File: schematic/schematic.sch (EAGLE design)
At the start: 24 parts, among them J2 SJ-2523-SMT-TR

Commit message: Audio recording schematic update
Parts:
- added MICRO_SD_MODULE: (no value), pinhead:PINHD-1X6
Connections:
- removed net N$2: J2.TIP, U$1.L
- new net AUDIO: ARDUINO_NANO_AUDIO_CONTROLLER.A7, J2.TIP, U$1.L
- new net AUDIO_PASS: ARDUINO_NANO_AUDIO_CONTROLLER.D9
- new net MISO: ARDUINO_NANO_AUDIO_CONTROLLER.D12, MICRO_SD_MODULE.4
- new net MOSI: ARDUINO_NANO_AUDIO_CONTROLLER.D11, MICRO_SD_MODULE.3
- new net SCK: ARDUINO_NANO_AUDIO_CONTROLLER.D13, MICRO_SD_MODULE.2
- new net SS: ARDUINO_NANO_AUDIO_CONTROLLER.D10, MICRO_SD_MODULE.1
- net GND: now also MICRO_SD_MODULE.6
- net VCC: now also MICRO_SD_MODULE.5
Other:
- moved on the sheet: ARDUINO_NANO_AUDIO_CONTROLLER

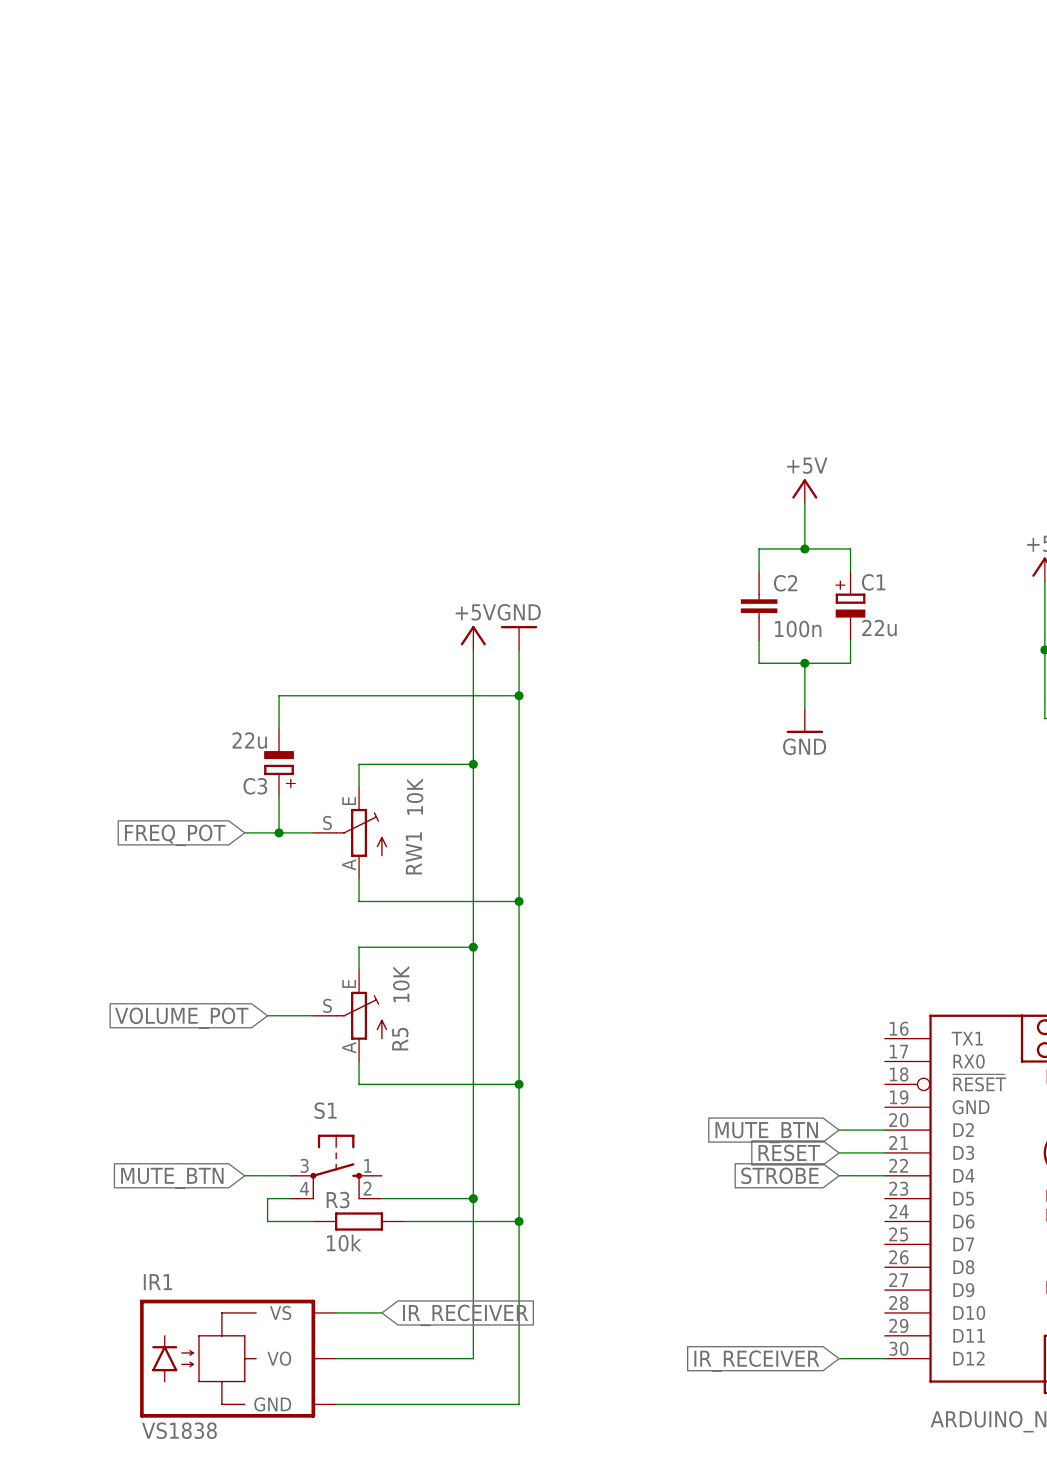
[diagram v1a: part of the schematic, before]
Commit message: Updated schematic with start/stop recording buttons
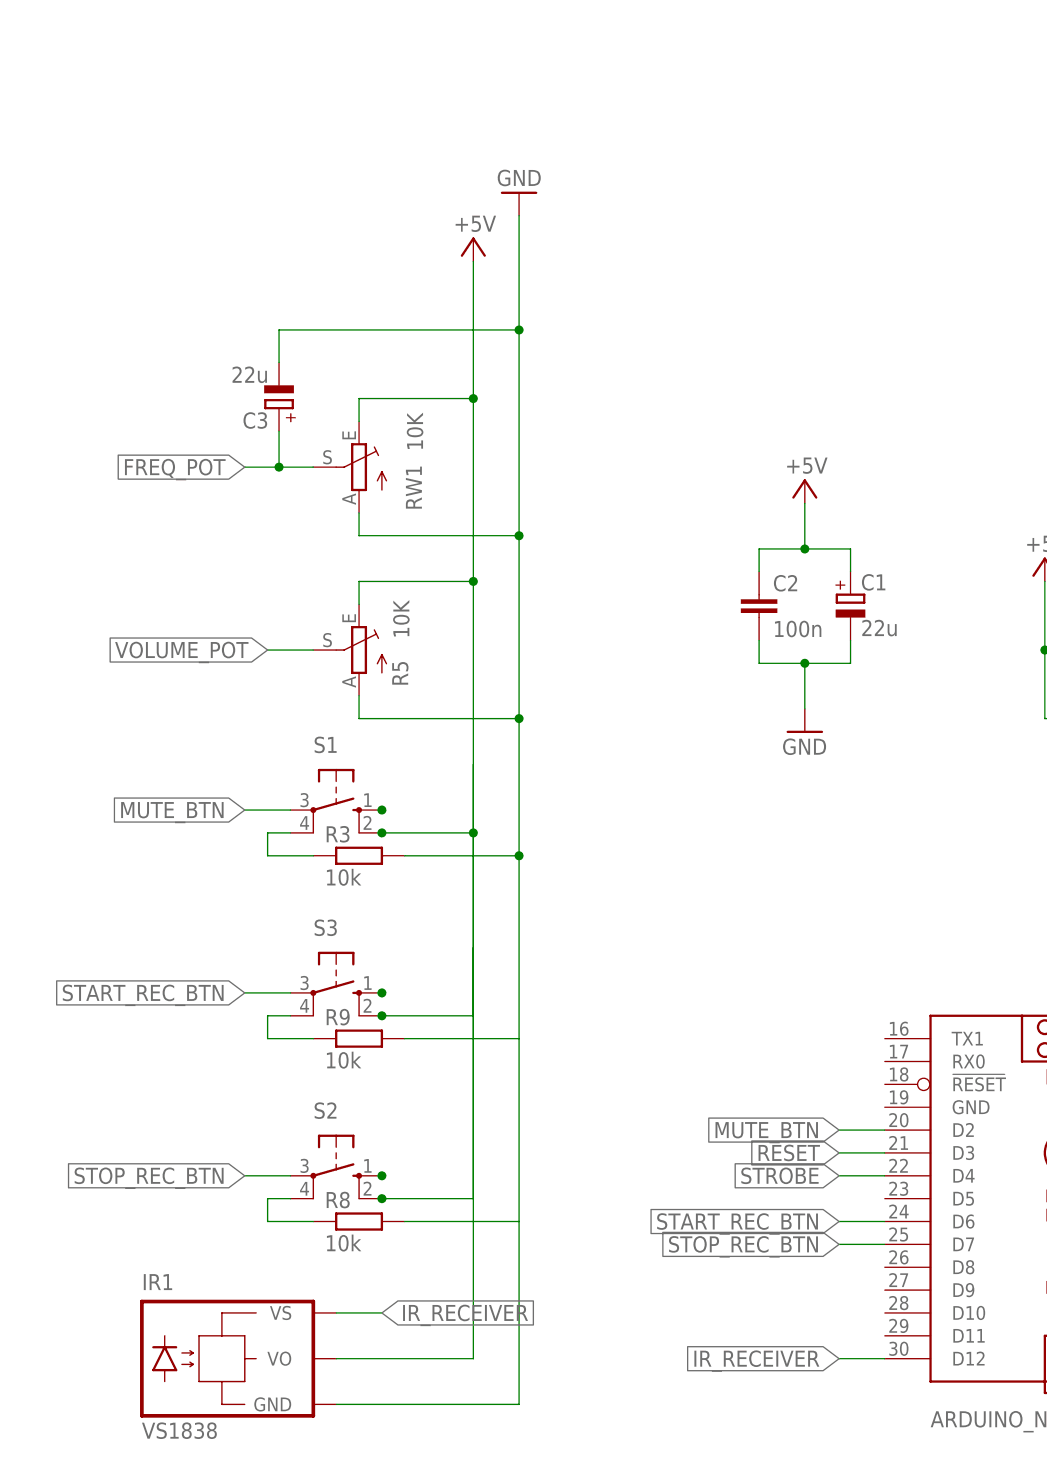
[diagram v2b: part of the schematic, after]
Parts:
- added R8, R9: 10k, rcl:R-EU_0204/7
- added S2, S3: (no value), switch-omron:10-XX
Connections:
- new net GND1: R8.2
- new net GND2: R9.2
- new net N$2: S2.S
- new net N$8: S3.S
- new net START_REC_BTN: ARDUINO_NANO_USER_CONTROLLER.D6, R9.1, S3.P, S3.P1, S3.S1
- new net STOP_REC_BTN: ARDUINO_NANO_USER_CONTROLLER.D7, R8.1, S2.P, S2.P1, S2.S1
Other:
- moved on the sheet: C3, R3, R5, RW1, S1

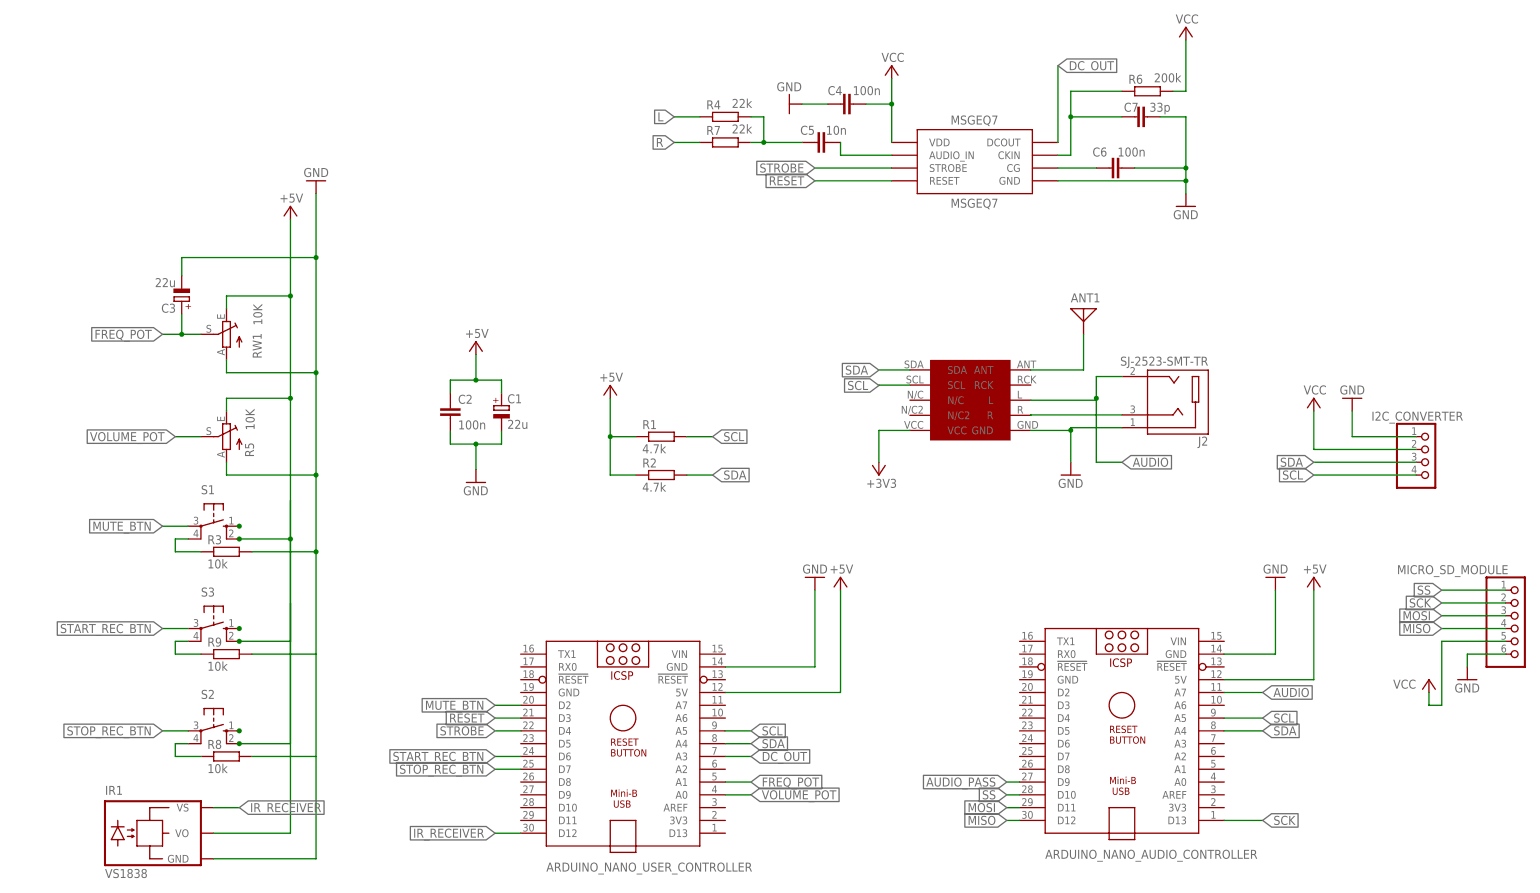
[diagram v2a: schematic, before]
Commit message: Update schematic visually
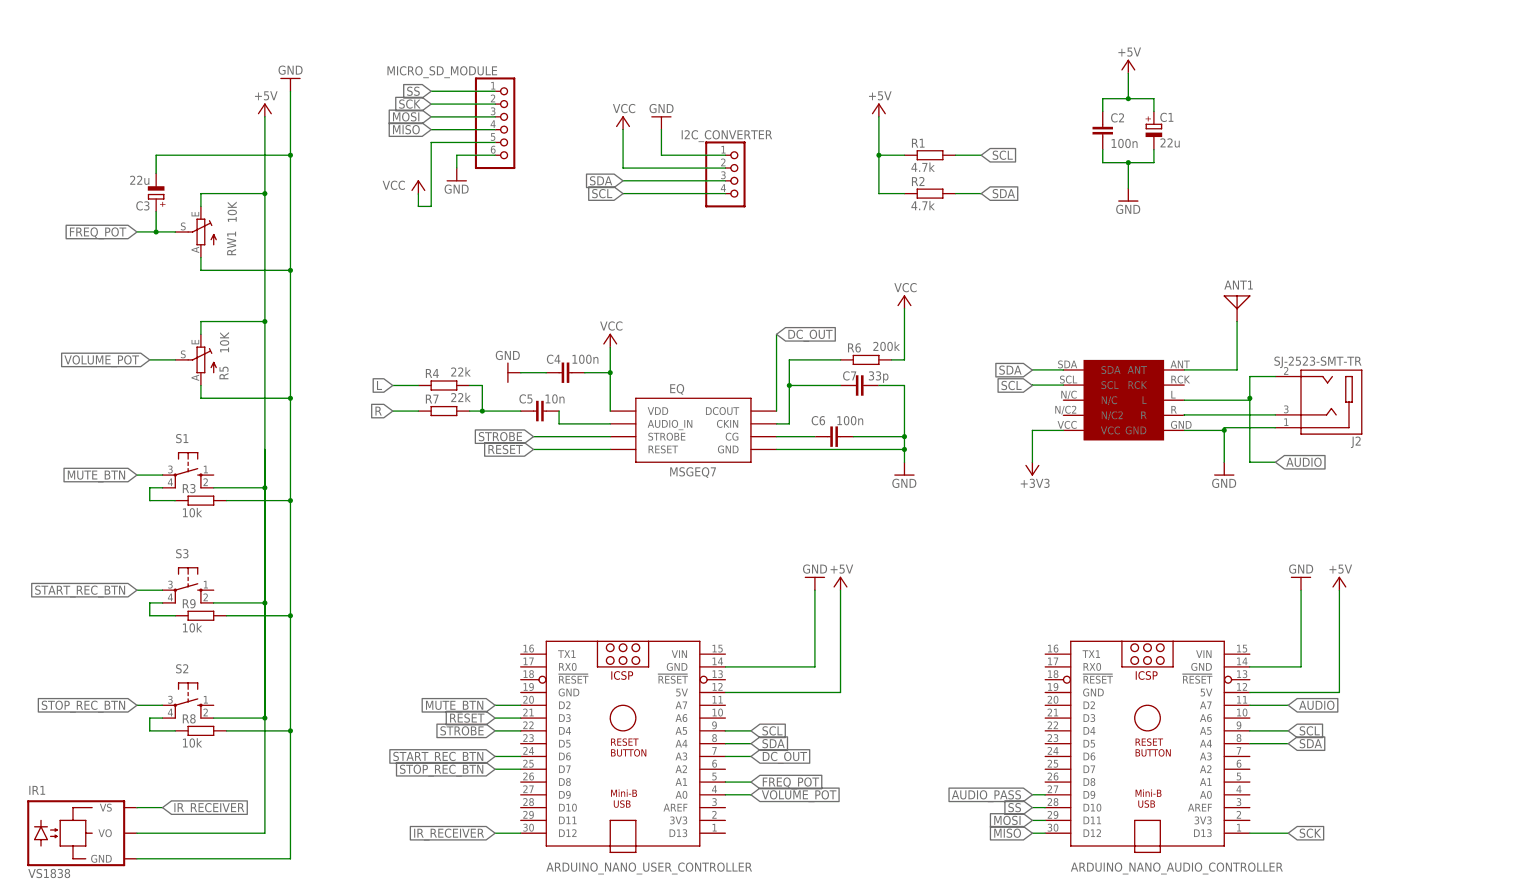
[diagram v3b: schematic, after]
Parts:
- removed MSGEQ7: MSGEQ7DIP, msgeq7:MSGEQ7DIP
- added EQ: MSGEQ7DIP, msgeq7:MSGEQ7DIP
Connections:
- removed net GND1: R8.2
- removed net GND2: R9.2
- new net +5V2: IR1.VO, R5.E, RW1.E, S1.S1, S2.S1, S3.S1
- new net N$9: R3.1, S1.P1
- net +5V: no longer IR1.VO, R5.E, RW1.E, S1.S
- net DC_OUT: now also EQ.DCOUT; no longer MSGEQ7.DCOUT
- net GND: now also EQ.GND, R8.2, R9.2; no longer MSGEQ7.GND
- net MUTE_BTN: no longer R3.1, S1.P1, S1.S1
- net N$2: now also R8.1, S2.P1; no longer S2.S
- net N$5: now also EQ.CKIN; no longer MSGEQ7.CKIN
- net N$6: now also EQ.AUDIO_IN; no longer MSGEQ7.AUDIO_IN
- net N$7: now also EQ.CG; no longer MSGEQ7.CG
- net N$8: now also R9.1, S3.P1; no longer S3.S
- net RESET: now also EQ.RESET; no longer MSGEQ7.RESET
- net START_REC_BTN: no longer R9.1, S3.P1, S3.S1
- net STOP_REC_BTN: no longer R8.1, S2.P1, S2.S1
- net STROBE: now also EQ.STROBE; no longer MSGEQ7.STROBE
- net VCC: now also EQ.VDD; no longer MSGEQ7.VDD
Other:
- moved on the sheet: ANT1, ARDUINO_NANO_AUDIO_CONTROLLER, C1, C2, C3, C4, C5, C6, C7, I2C_CONVERTER, IR1, J2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
